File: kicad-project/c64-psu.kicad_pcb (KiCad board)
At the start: 2 copper layers, 122 x 74 mm, 75 parts, among them J1 Conn_01x02, J2 Conn_01x02, J3 Conn_01x02, Q1 N-MOS, U1 MAX6399, U2 LMR33630A

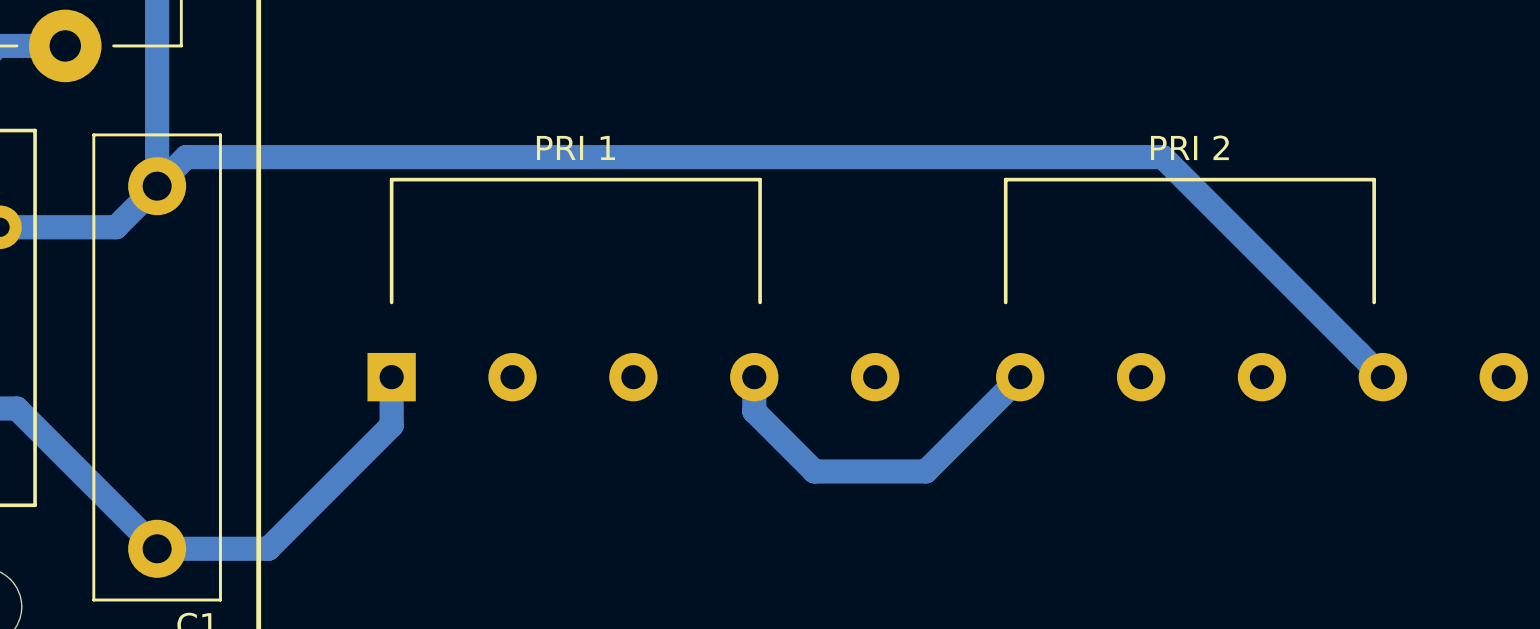
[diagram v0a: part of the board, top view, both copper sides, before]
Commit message: fix TR1 primary series connection (!!!), added voltage threshold comments on schematic, reversed J3 (when did that break?), added test captures,
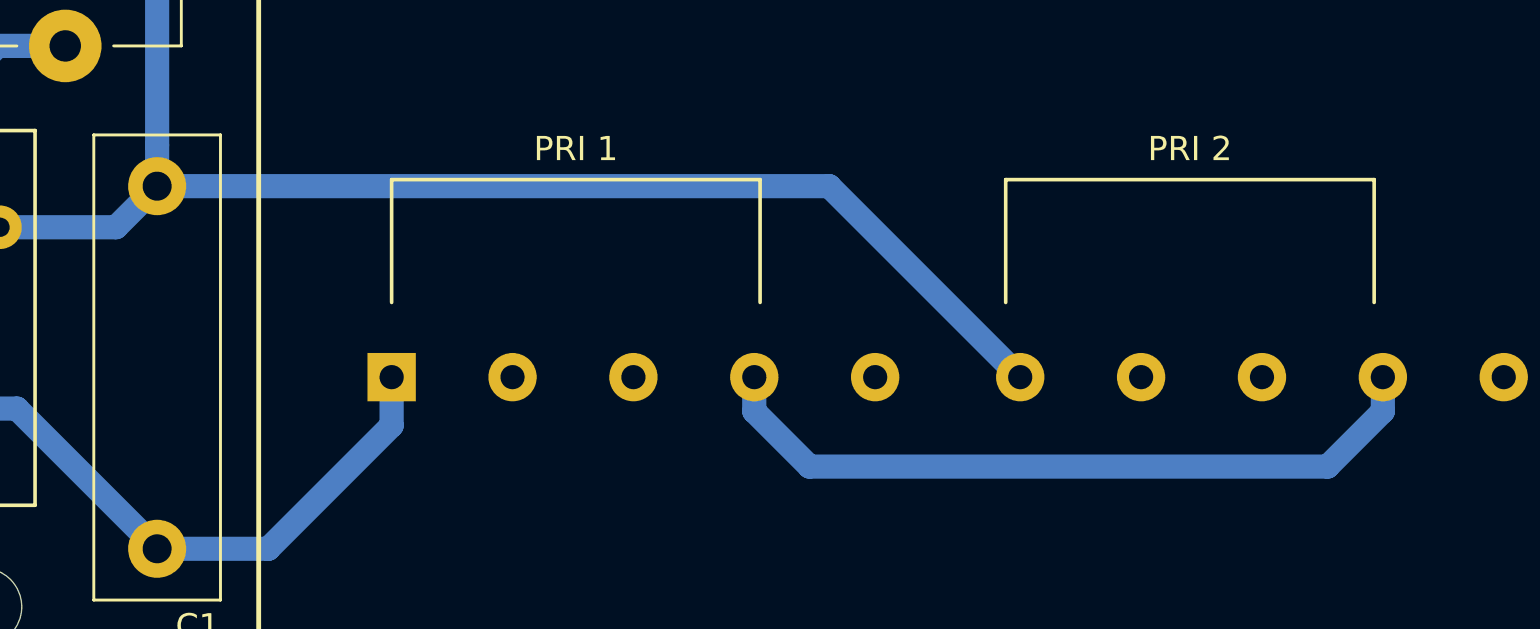
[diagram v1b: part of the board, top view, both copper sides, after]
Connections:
- C1 pad 2: /PRI2B -> /PRI2A
- J1 pad 1: /PRI2B -> /PRI2A
- RV3 pad 2: /PRI2B -> /PRI2A
- TR1 pad 6: /PRI1B -> /PRI2A
- TR1 pad 9: /PRI2B -> /PRI1B
- U1 pad 9: GND -> (no net)
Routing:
- net /PRI2B: track 104.0 -> 0.00 mm
- net /PRI2A: track 0.00 -> 88.0 mm
- net /PRI1B: track 15.1 -> 30.7 mm
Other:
- board text added: "Use the sch -> export netlist -> pcb -> load netlist instead of the new “update pcb from schematic”, or the stitching vias will be lost"

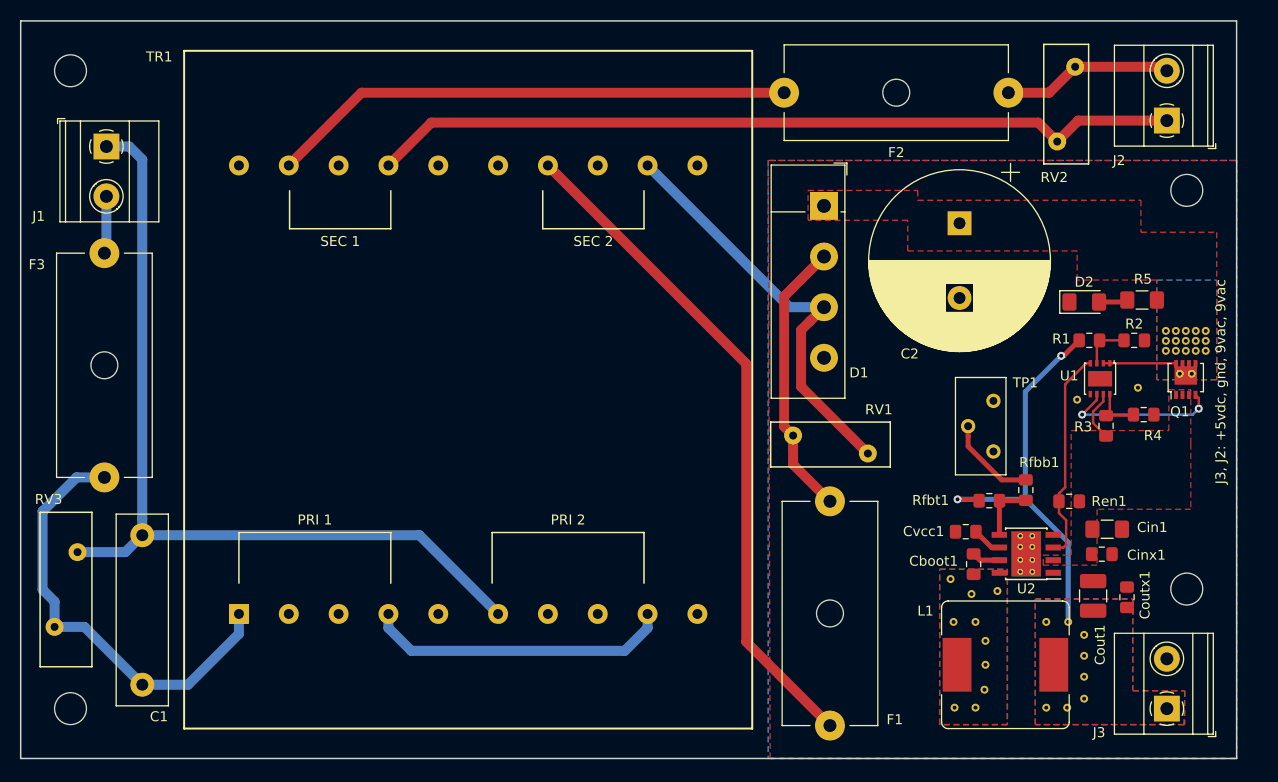
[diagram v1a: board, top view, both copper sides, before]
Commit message: HF noise improvements (reduce high di/dt loop area, reduce SW node area, etc.).
Also:

+ Moved trf's origin to pin 1
+ Replaced 5 mm pitch connectors with (apparently safer) 7.62 mm

ToDo:

- Could be further improved by fitting the switcher between the filter cap legs on the bottom side! Will try that next.
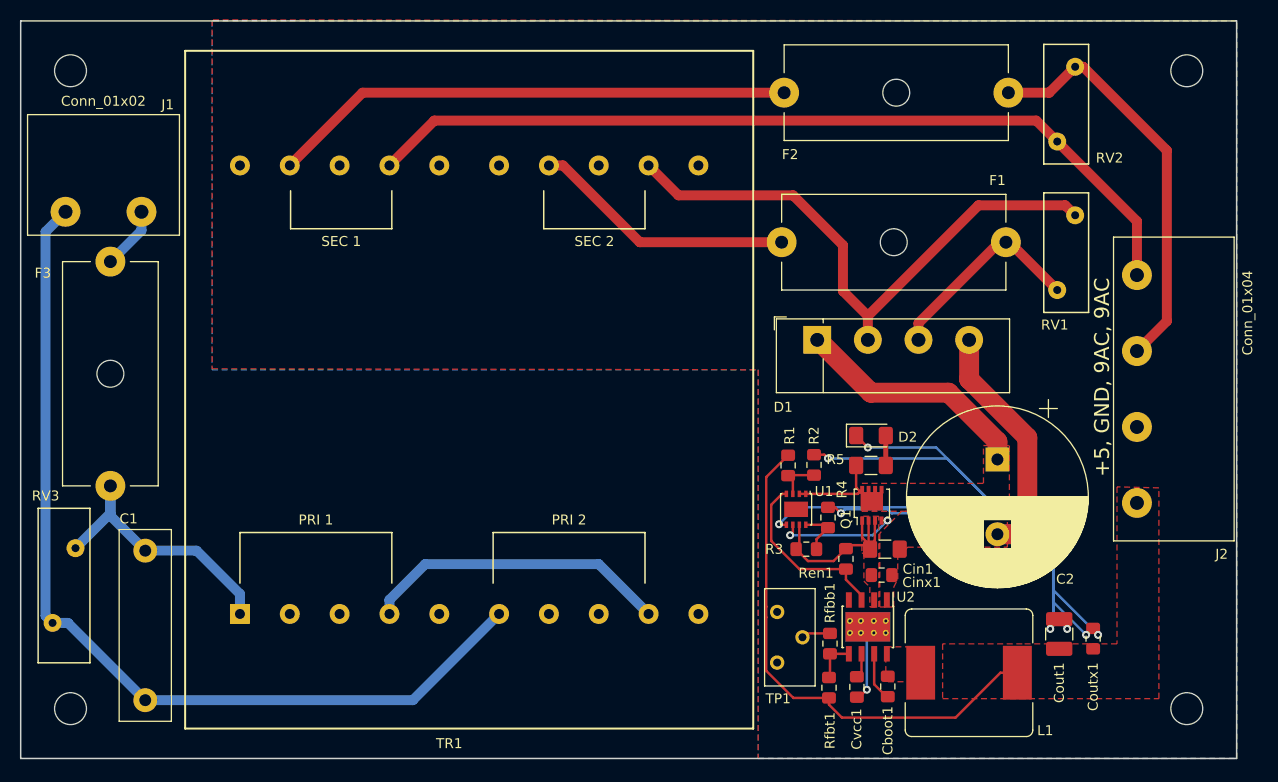
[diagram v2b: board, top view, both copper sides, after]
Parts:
- removed G***: LOGO, c64-psu:linkballoon
- removed J3: Conn_01x02, TerminalBlock_Phoenix:TerminalBlock_Phoenix_MKDS-1,5-2_1x02_P5.00mm_Horizontal
- removed REF** (x37): Via-0.4mm, c64-psu:Via-0.4mm
- added NT1: Net-Tie_2, NetTie:NetTie-2_THT_Pad1.0mm, F.Cu at (190.0, 113.5)
- J1: footprint TerminalBlock_Phoenix:TerminalBlock_Phoenix_MKDS-1,5-2_1x02_P5.00mm_Horizontal -> c64-psu:KF7.62_2P
- J2: value Conn_01x02 -> Conn_01x04; footprint TerminalBlock_Phoenix:TerminalBlock_Phoenix_MKDS-1,5-2_1x02_P5.00mm_Horizontal -> c64-psu:KF7.62_4P
- R5: value 10k -> 4K7
- moved TR1 45.0 mm to (111.0, 121.5)
- moved R2 34.5 mm to (168.6, 106.5), turned to 90 degrees
- moved Q1 33.9 mm to (174.4, 110.6)
- moved R4 33.3 mm to (170.0, 111.8), turned to 90 degrees
- moved U1 33.2 mm to (166.8, 111.0)
- moved R1 32.7 mm to (166.0, 106.6), turned to 270 degrees
- moved R3 32.5 mm to (167.8, 115.0), turned to 0 degrees
- moved R5 31.9 mm to (174.3, 106.6), turned to 0 degrees
- moved RV1 31.7 mm to (194.8, 81.5), turned to 270 degrees
- moved F1 31.4 mm to (187.8, 84.2), turned to 180 degrees
- moved TP1 27.0 mm to (164.9, 121.3), turned to 90 degrees
- moved D2 25.2 mm to (174.3, 103.6)
- moved Rfbb1 25.0 mm to (170.2, 124.5)
- moved Rfbt1 24.7 mm to (170.1, 128.9), turned to 90 degrees
- moved C2 24.0 mm to (187.0, 106.0)
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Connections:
- C2 pad 2: GND -> GNDPWR
- Cin1 pad 2: GND -> GNDPWR
- Cinx1 pad 2: GND -> GNDPWR
- D1 pad 2: Net-(D1-Pad2) -> /SEC2B
- D1 pad 3: /SEC2B -> Net-(D1-Pad3)
- D1 pad 4: GND -> GNDPWR
- F1 pad 1: Net-(D1-Pad2) -> Net-(D1-Pad3)
- RV1 pad 2: Net-(D1-Pad2) -> Net-(D1-Pad3)
- U2 pad 1: GND -> GNDPWR
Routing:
- net GND: track 0.00 -> 161.1 mm, vias 0 -> 9
- net /SEC2A: track 67.9 -> 26.5 mm
- net Net-(D1-Pad2): track 28.1 -> 0.00 mm
- net GNDPWR: track 0.00 -> 27.9 mm
- net /Vd: track 7.32 -> 34.9 mm
- net Net-(F2-Pad1): track 17.1 -> 41.8 mm
- net Net-(D1-Pad3): track 0.00 -> 21.0 mm
- net /SEC2B: track 42.0 -> 59.2 mm
- net /PRI1A: track 44.7 -> 29.0 mm
- net /VIN: track 5.16 -> 19.1 mm
- net /VOUT: track 41.4 -> 51.9 mm, vias 2 -> 0
- net Net-(Rfbb1-Pad2): track 9.21 -> 2.92 mm
- net /PRI2A: track 88.0 -> 94.0 mm
- net /SEC1B: track 81.5 -> 86.4 mm
- net Net-(Q1-Pad2): track 16.1 -> 12.2 mm
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- added copper zone on F.Cu, net GNDPWR
- removed copper zone on B.Cu, net /SW
- removed copper zone on B.Cu, net /VOUT
- removed copper zone on B.Cu, net /Vd
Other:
- net class huge added: clearance 0.254, trace_width 2, via_dia 0.8, via_drill 0.4
- net class maxpow: clearance 0.4 -> 0.254
- net class pow: clearance 0.4 -> 0.254
- board text added: "+5, GND, 9AC, 9AC"
- board text removed: "J3, J2: +5vdc, gnd, 9vac, 9vac"
- board text removed: "Use the sch -> export netlist -> pcb -> load netlist instead of the new “update pcb from schematic”, or the stitching vias will be lost"

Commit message: v2018.2 ready for mfr
+ replaced terminal blocks with quick-disconnect / spade connectors +
+ added footprints for fuses
+ enclosure redone in fusion 3d (sorry freecad 0.17 bodies are not mature yet, I tried)
+ gerbers ready for prod
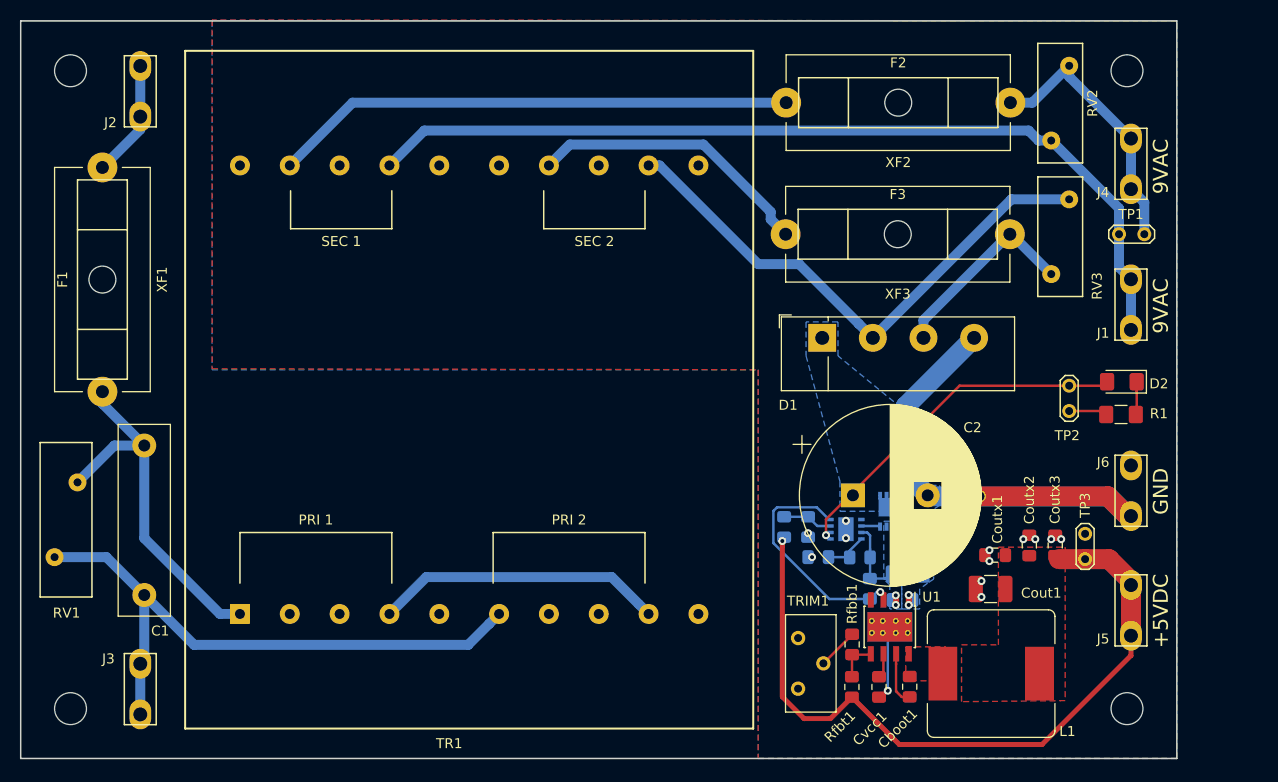
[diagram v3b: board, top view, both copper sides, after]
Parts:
- added Coutx2: 1u, Capacitor_SMD:C_0805_2012Metric_Pad1.15x1.40mm_HandSolder, F.Cu at (190.2, 114.6)
- added Coutx3: 1u, Capacitor_SMD:C_0805_2012Metric_Pad1.15x1.40mm_HandSolder, F.Cu at (192.8, 114.6)
- added G***: LOGO, c64-psu:linkballoon, B.Cu at (151.8, 94.4)
- added J3: Conn_01x01, c64-psu:spade_4.8mm, F.Cu at (101.0, 131.6)
- added J4: Conn_01x01, c64-psu:spade_4.8mm, F.Cu at (200.4, 78.9)
- added J5: Conn_01x01, c64-psu:spade_4.8mm, F.Cu at (200.4, 123.7)
- added J6: Conn_01x01, c64-psu:spade_4.8mm, F.Cu at (200.4, 111.7)
- added TP2: TestPoint_2Pole, TestPoint:TestPoint_2Pads_Pitch2.54mm_Drill0.8mm, F.Cu at (194.2, 98.6)
- added TP3: TestPoint_2Pole, TestPoint:TestPoint_2Pads_Pitch2.54mm_Drill0.8mm, F.Cu at (195.8, 116.0)
- added TRIM1: 10K, Potentiometer_THT:Potentiometer_Bourns_3296Y_Vertical, F.Cu at (167.0, 123.9)
- added XF1: 160 mA, Fuse:Fuseholder_Cylinder-5x20mm_Schurter_0031_8201_Horizontal_Open, F.Cu at (97.2, 76.7)
- added XF2: Fuse Holder, Fuse:Fuseholder_Cylinder-5x20mm_Schurter_0031_8201_Horizontal_Open, F.Cu at (188.3, 70.2)
- added XF3: 1.67A, Fuse:Fuseholder_Cylinder-5x20mm_Schurter_0031_8201_Horizontal_Open, F.Cu at (188.2, 83.4)
- Cin1, Cinx1, Q1, R3, Ren1: moved to B.Cu
- F1: value 1.67A -> 160mA; footprint Fuse:Fuseholder_Cylinder-5x20mm_Schurter_0031_8201_Horizontal_Open -> c64-psu:20mm fuse
- F2: footprint Fuse:Fuseholder_Cylinder-5x20mm_Schurter_0031_8201_Horizontal_Open -> c64-psu:20mm fuse
- F3: value 160mA -> 1.67A; footprint Fuse:Fuseholder_Cylinder-5x20mm_Schurter_0031_8201_Horizontal_Open -> c64-psu:20mm fuse
- J1: value Conn_01x02 -> Conn_01x01; footprint c64-psu:KF7.62_2P -> c64-psu:spade_4.8mm
- J2: value Conn_01x04 -> Conn_01x01; footprint c64-psu:KF7.62_4P -> c64-psu:spade_4.8mm
- R1: value 820k -> 4K7; footprint Resistor_SMD:R_0805_2012Metric_Pad1.15x1.40mm_HandSolder -> Resistor_SMD:R_1206_3216Metric_Pad1.42x1.75mm_HandSolder
- R2: value 68k -> 820k; moved to B.Cu
- R4: value 150k -> 68k; moved to B.Cu
- R5: value 4K7 -> 150k; footprint Resistor_SMD:R_1206_3216Metric_Pad1.42x1.75mm_HandSolder -> Resistor_SMD:R_0805_2012Metric_Pad1.15x1.40mm_HandSolder; moved to B.Cu
- RV1: value S10K20 -> S14K300; footprint Varistor:RV_Disc_D12mm_W4.5mm_P7.5mm -> Varistor:RV_Disc_D15.5mm_W5.2mm_P7.5mm
- RV3: value S14K300 -> S10K20; footprint Varistor:RV_Disc_D15.5mm_W5.2mm_P7.5mm -> Varistor:RV_Disc_D12mm_W4.5mm_P7.5mm
- TP1: value 10K -> TestPoint_2Pole; footprint Potentiometer_THT:Potentiometer_Bourns_3296Y_Vertical -> TestPoint:TestPoint_2Pads_Pitch2.54mm_Drill0.8mm
- U1: value MAX6399 -> LMR33630A; footprint Package_DFN_QFN:DFN-8-1EP_3x3mm_P0.65mm_EP1.55x2.4mm -> Package_SO:TI_SO-PowerPAD-8_ThermalVias
- U2: value LMR33630A -> MAX6399; footprint Package_SO:TI_SO-PowerPAD-8_ThermalVias -> Package_DFN_QFN:DFN-8-1EP_3x3mm_P0.65mm_EP1.55x2.4mm; moved to B.Cu
- moved J1 107.6 mm to (200.4, 93.0), turned to 90 degrees
- moved RV3 105.7 mm to (194.2, 79.9)
- moved RV1 103.6 mm to (94.7, 108.3)
- moved J2 101.3 mm to (101.0, 71.6), turned to 90 degrees
- moved F1 90.7 mm to (97.2, 88.0), turned to 270 degrees
- moved F3 82.9 mm to (177.0, 83.4), turned to 180 degrees
- moved TP1 51.1 mm to (199.2, 83.4), turned to 0 degrees
- moved R1 33.8 mm to (199.4, 101.5), turned to 180 degrees
- moved D2 25.7 mm to (199.5, 98.2), turned to 180 degrees
- moved U1 15.1 mm to (176.2, 122.8)
- moved C2 14.9 mm to (172.5, 109.6), turned to 0 degrees
- moved Coutx1 12.9 mm to (186.8, 115.6), turned to 180 degrees
- moved F2 11.1 mm to (177.1, 70.2)
- moved R5 10.6 mm to (169.0, 115.8), turned to 180 degrees
- moved C1 10.6 mm to (101.4, 104.6)
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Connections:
- D2 pad 1: GND -> Net-(D2-Pad1)
- D2 pad 2: Net-(D2-Pad2) -> /Vd
- J1 pad 1: /PRI2A -> /SEC1B
- J2 pad 1: /SEC1B -> Net-(J2-Pad1)
- Q1 pad 2: Net-(Q1-Pad2) -> /Gate
- R1 pad 1: /VOUT -> Net-(D2-Pad1)
- R1 pad 2: Net-(R1-Pad2) -> GND
- R2 pad 1: Net-(R1-Pad2) -> /VOUT
- R2 pad 2: GND -> Net-(R2-Pad2)
- R4 pad 1: Net-(R3-Pad2) -> Net-(R2-Pad2)
- R5 pad 1: /Vd -> Net-(R3-Pad2)
- R5 pad 2: Net-(D2-Pad2) -> GND
- RV1 pad 1: /SEC2B -> /PRI1A
- RV1 pad 2: Net-(D1-Pad3) -> /PRI2A
- RV2 pad 2: Net-(F2-Pad1) -> Net-(J4-Pad1)
- RV3 pad 1: /PRI1A -> /SEC2B
- RV3 pad 2: /PRI2A -> Net-(D1-Pad3)
- TP1 pad 1: Net-(TP1-Pad1) -> /SEC1B
- TP1 pad 2: Net-(Rfbb1-Pad2) -> Net-(J4-Pad1)
- U1 pad 1: /Vd -> GNDPWR
- U1 pad 2: /Vd -> /VIN
- U1 pad 3: Net-(R1-Pad2) -> Net-(Ren1-Pad1)
- U1 pad 4: Net-(Ren1-Pad1) -> Net-(U1-Pad4)
- U1 pad 5: GND -> Net-(Rfbb1-Pad1)
- U1 pad 6: Net-(Q1-Pad2) -> Net-(Cvcc1-Pad1)
- U1 pad 7: /VIN -> Net-(Cboot1-Pad1)
- U1 pad 8: Net-(R3-Pad2) -> /SW
- U1 pad 9: (no net) -> GND
- U2 pad 1: GNDPWR -> /Vd
- U2 pad 2: /VIN -> /Vd
- U2 pad 3: Net-(Ren1-Pad1) -> Net-(R2-Pad2)
- U2 pad 4: Net-(U2-Pad4) -> Net-(Ren1-Pad1)
- U2 pad 5: Net-(Rfbb1-Pad1) -> GND
- U2 pad 6: Net-(Cvcc1-Pad1) -> /Gate
- U2 pad 7: Net-(Cboot1-Pad1) -> /VIN
- U2 pad 8: /SW -> Net-(R3-Pad2)
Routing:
- net GND: track 161.1 -> 44.6 mm, vias 9 -> 13
- net Net-(F2-Pad1): track 41.8 -> 0.00 mm
- net /PRI2A: track 94.0 -> 61.7 mm
- net Net-(J4-Pad1): track 0.00 -> 27.5 mm
- net /VOUT: track 51.9 -> 75.2 mm, vias 0 -> 1
- net Net-(Q1-Pad2): track 12.2 -> 0.00 mm, vias 2 -> 0
- net Net-(J2-Pad1): track 0.00 -> 11.8 mm
- net /VIN: track 19.1 -> 7.96 mm, vias 0 -> 2
- net /PRI1A: track 29.0 -> 37.4 mm
- net Net-(F3-Pad2): track 6.29 -> 0.00 mm
- net Net-(Ren1-Pad1): track 18.0 -> 23.9 mm, vias 0 -> 1
- net GNDPWR: track 27.9 -> 22.2 mm, vias 0 -> 2
- net Net-(R2-Pad2): track 0.00 -> 5.03 mm
- net Net-(R1-Pad2): track 4.64 -> 0.00 mm
- net /SEC1B: track 86.4 -> 90.6 mm
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- added copper zone on B.Cu, net /VIN
- added copper zone on B.Cu, net /Vd
- added copper zone on B.Cu, net GNDPWR
- removed copper zone on F.Cu, net /VIN
- removed copper zone on F.Cu, net /Vd
- removed copper zone on F.Cu, net GNDPWR
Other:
- board size 122 x 74 mm -> 116 x 74 mm
- board text added: "+5VDC"
- board text added: "9VAC"
- board text added: "GND"
- board text added: "v2018.2"
- board text removed: "+5, GND, 9AC, 9AC"
